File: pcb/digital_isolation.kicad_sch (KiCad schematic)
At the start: 4 parts, among them U10 ISO7740, U19 ISO7740, U22 ISO7742

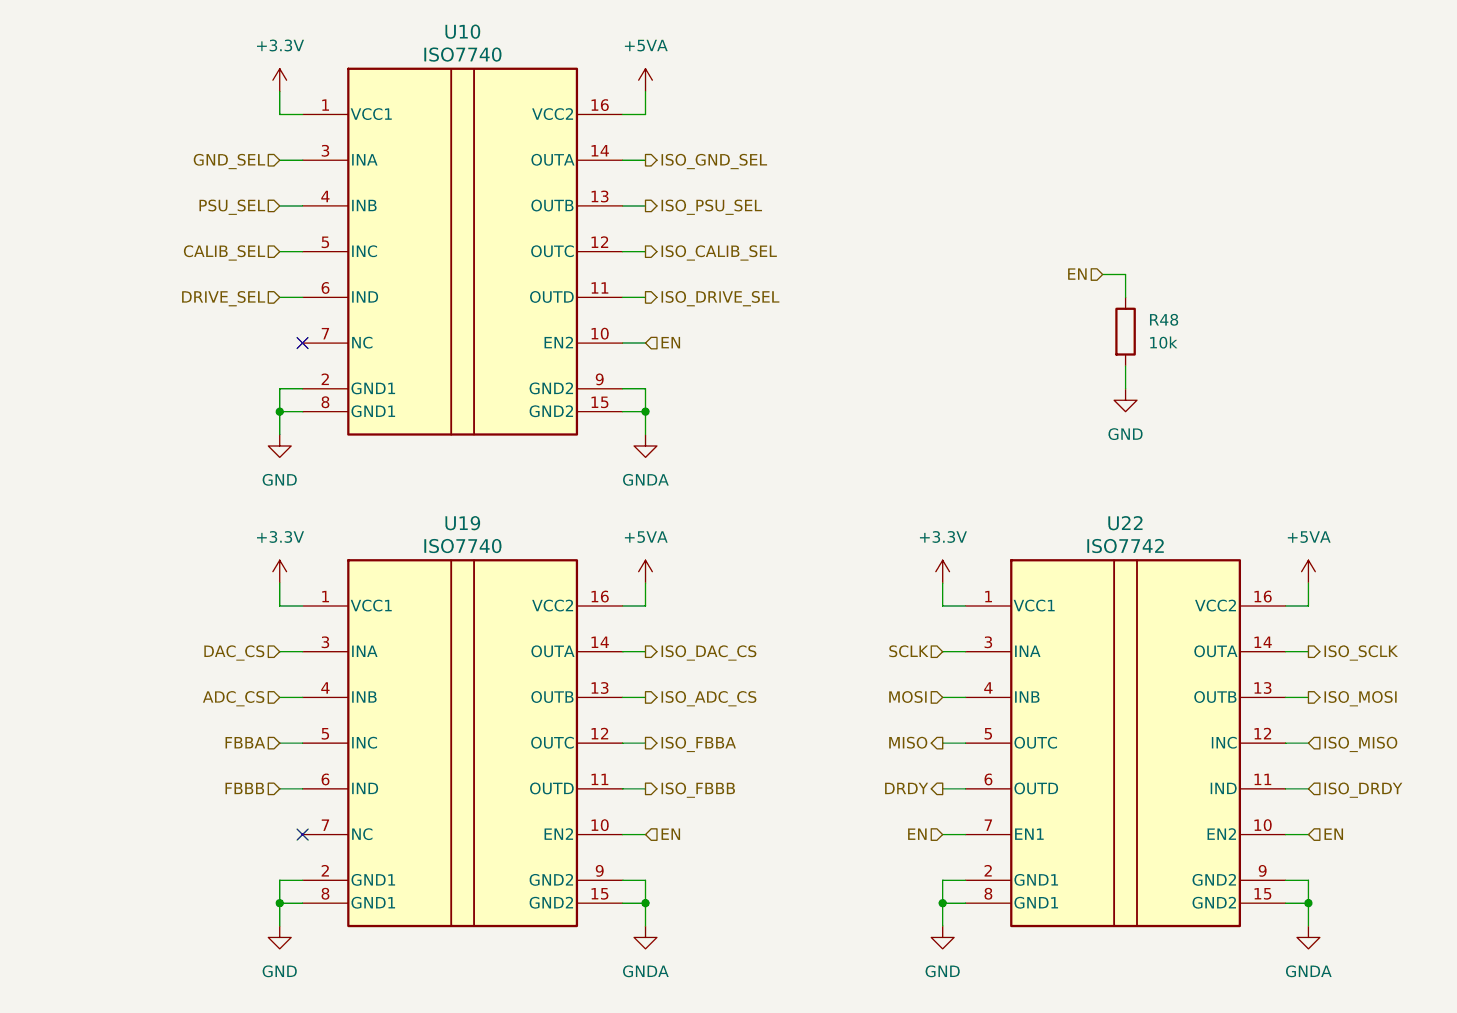
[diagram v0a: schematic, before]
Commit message: reworked the digital isolation block
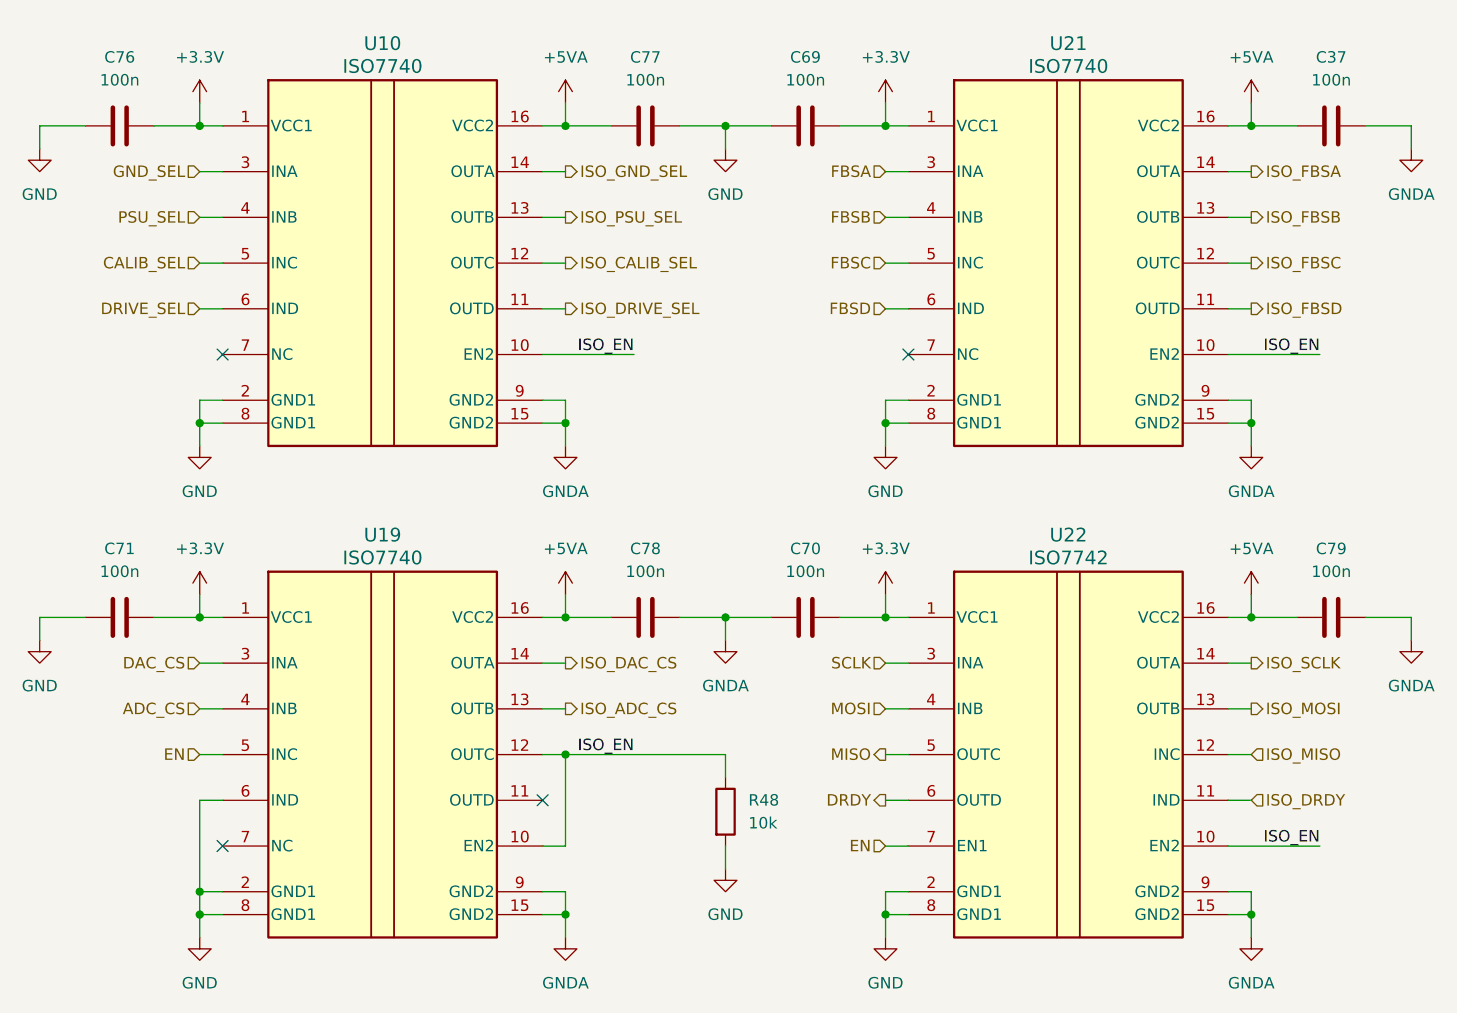
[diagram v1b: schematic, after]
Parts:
- added C37, C69, C70, C71, C76, C77, C78, C79: 100n, symbol Device:C
- added U21: ISO7740, DBQ0016A_N, symbol project_library:ISO7740
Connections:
- net FBBA is gone; now on net EN: U19.5 (INC)
- net FBBB is gone; now on net GND: U19.6 (IND)
- net +3.3V: now also C69.2, C70.2, C71.2, C76.2, U21.1 (VCC1)
- net +5VA: now also C37.1, C77.1, C78.1, C79.1, U21.16 (VCC2)
- net EN: no longer R48.1, U10.10 (EN2), U19.10 (EN2), U22.10 (EN2)
- net GND: now also C69.1, C71.1, C76.1, C77.2, U21.2 (GND1), U21.8 (GND1)
- net GNDA: now also C37.2, C70.1, C78.2, C79.2, U21.15 (GND2), U21.9 (GND2)
- net ISO_FBBA renamed ISO_EN
- net ISO_EN: now also R48.1, U10.10 (EN2), U19.10 (EN2), U22.10 (EN2), U21.10 (EN2)
- net ISO_FBBB: no longer names the net of U19.11 (OUTD)
- new net FBSA: U21.3 (INA)
- new net FBSB: U21.4 (INB)
- new net FBSC: U21.5 (INC)
- new net FBSD: U21.6 (IND)
- new net ISO_FBSA: U21.14 (OUTA)
- new net ISO_FBSB: U21.13 (OUTB)
- new net ISO_FBSC: U21.12 (OUTC)
- new net ISO_FBSD: U21.11 (OUTD)
- no-connect marks 2 -> 4
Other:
- title: (none) -> Digital Isolation for Analog Zone
- moved on the sheet: R48, U10, U19, U22

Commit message: rework to tia feedback selection, board power, and ui
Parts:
- removed C76, C77: 100n, symbol Device:C
- removed U10: ISO7740, DBQ0016A_N, symbol project_library:ISO7740
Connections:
- net FBSA renamed ~{FBSA}
- net FBSB renamed ~{FBSB}
- net FBSC renamed ~{FBSC}
- net FBSD renamed ~{FBSD}
- net ISO_FBSA renamed ~{ISO_FBSA}
- net ISO_FBSB renamed ~{ISO_FBSB}
- net ISO_FBSC renamed ~{ISO_FBSC}
- net ISO_FBSD renamed ~{ISO_FBSD}
- no-connect marks 4 -> 3
